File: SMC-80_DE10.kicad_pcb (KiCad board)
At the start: 4 copper layers, 51.8 x 47.2 mm, 32 parts, among them J1 IDE, J2 Port A, J3 Arduino1, J4 DE10-Lite GPIO, J5 Arduino2, U1 SST39SF040, U2 Z84C0010AEG, U3 AS6C4008A-55ZIN, U4 Z84C4310AEG

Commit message: rotated layout
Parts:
- removed the C1 at (205.7, 121.5)
- removed the D1 at (204.5, 114.7)
- removed the J1 at (128.6, 84.1)
- removed the J2 at (161.2, 121.0)
- removed JP1: IDE PWR, Connector_PinHeader_2.54mm:PinHeader_1x02_P2.54mm_Vertical
- removed JP2: WR Ena, Connector_PinHeader_2.54mm:PinHeader_1x03_P2.54mm_Vertical
- removed the R1 at (221.5, 113.8)
- removed the R2 at (225.3, 121.4)
- removed the R3 at (216.3, 122.8)
- removed the R5 at (204.1, 112.3)
- removed RN1: 2K2, Resistor_SMD:R_Cat16-4
- added J4: Port A, Connector_PinHeader_2.54mm:PinHeader_1x06_P2.54mm_Vertical, F.Cu at (114.3, 91.4)
- added R10: 10K, Resistor_SMD:R_0603_1608Metric_Pad1.05x0.95mm_HandSolder, F.Cu at (166.4, 110.5)
- added R7: 10K, Resistor_SMD:R_0603_1608Metric_Pad1.05x0.95mm_HandSolder, F.Cu at (138.4, 119.4)
- added R9: 10K, Resistor_SMD:R_0603_1608Metric_Pad1.05x0.95mm_HandSolder, F.Cu at (149.9, 111.8)
- R4: value 10K -> 100K
- R8: value 100K -> 10K
- RN2: value 10K -> 2K2
- U4: moved to F.Cu
- moved R4 97.6 mm to (116.8, 94.0), turned to 180 degrees
- moved R6 87.6 mm to (127.0, 94.0), turned to 0 degrees
- moved C5 80.5 mm to (123.2, 96.5)
- moved D1 77.2 mm to (139.7, 91.4), turned to 180 degrees
- moved R3 69.4 mm to (129.5, 133.9), turned to 180 degrees
- moved R5 67.5 mm to (127.0, 96.5), turned to 180 degrees
- moved R1 66.8 mm to (143.5, 91.4)
- moved R8 60.2 mm to (138.4, 116.8)
- moved C4 55.1 mm to (129.5, 119.4)
- moved C3 53.7 mm to (134.6, 105.4), turned to 180 degrees
- moved U4 49.9 mm to (120.7, 105.4)
- moved J1 44.1 mm to (170.5, 140.1), turned to 0 degrees
- moved RN2 43.1 mm to (110.5, 99.1)
- moved R2 42.3 mm to (156.2, 134.6), turned to 180 degrees
- moved U1 41.5 mm to (143.5, 130.8)
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- renumbered C2 to C1, C3 to C2, C4 to C3, C5 to C4, C6 to C5, D2 to D1, J3 to J1, J4 to J2, J5 to J3, R7 to R1, R9 to R2, R10 to R3, R11 to R5
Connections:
- J1 pad 1: /~M1 -> Net-(J1-Pad1)
- J1 pad 10: /SIO_~CE -> /~MREQ
- J1 pad 2: /~MREQ -> Net-(J1-Pad2)
- J1 pad 5: /~IORQ -> Net-(J1-Pad5)
- J1 pad 6: /~HALT -> /A16
- J1 pad 7: /~WAIT -> /A17
- J1 pad 8: Net-(J3-Pad8) -> /A18
- J1 pad 9: Net-(J3-Pad9) -> /~HALT
- J2 pad 2: /~RESET -> /ROM_~CE
- J2 pad 25: /A16 -> /D0
- J2 pad 26: /A17 -> /~RESET
- J2 pad 27: /A18 -> /D2
- J2 pad 28: /ROM_~CE -> /D1
- J2 pad 31: /D0 -> /D4
- J2 pad 32: /D1 -> /D3
- J2 pad 33: /D2 -> /D6
- J2 pad 34: /D3 -> /D5
- J2 pad 35: /D4 -> Net-(J2-Pad35)
- J2 pad 36: /D5 -> /D7
- J2 pad 37: /D6 -> Net-(J2-Pad37)
- J2 pad 38: /D7 -> /CLK
- J2 pad 39: /CLK -> /CLK_U
- J2 pad 40: /IDE_~CE~ -> /SIO_~CE
- J3 pad 1: /CLK_U -> /~IORQ
- J3 pad 2: Net-(J5-Pad2) -> /~WAIT
- J3 pad 3: Net-(J5-Pad3) -> /~M1
- J3 pad 5: /~RTS -> Net-(J3-Pad5)
- J3 pad 6: /RX -> Net-(J3-Pad6)
- J3 pad 7: /TX -> Net-(J3-Pad7)
- J3 pad 8: /~CTS -> Net-(J3-Pad8)
- R4 pad 1: VCC -> Net-(J4-Pad2)
- R4 pad 2: Net-(J1-Pad38) -> VCC
- R6 pad 1: Net-(J2-Pad2) -> Net-(J4-Pad6)
- R6 pad 2: VCC -> GND
- R8 pad 1: Net-(J2-Pad6) -> /Ram Rom and CPU/~INT
- R8 pad 2: GND -> VCC
- RN2 pad 1: VCC -> Net-(J4-Pad2)
- RN2 pad 2: VCC -> Net-(J4-Pad4)
- RN2 pad 3: VCC -> Net-(J4-Pad5)
- RN2 pad 4: VCC -> Net-(J4-Pad6)
- RN2 pad 5: /Ram Rom and CPU/~NMI -> /Ram Rom and CPU/~CTS
- RN2 pad 6: /~WAIT -> /Ram Rom and CPU/TXA
- RN2 pad 7: /Ram Rom and CPU/~BUSRQ -> /Ram Rom and CPU/RX
- RN2 pad 8: /Ram Rom and CPU/~INT -> /Ram Rom and CPU/~RTS
- U1 pad 31: Net-(JP2-Pad2) -> /~WR
- U4 pad 2: /~RTS -> /Ram Rom and CPU/~RTS
- U4 pad 3: /~CTS -> /Ram Rom and CPU/~CTS
- U4 pad 41: /RX -> /Ram Rom and CPU/RX
- U4 pad 44: /TX -> /Ram Rom and CPU/TXA
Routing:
- net /A1: track 0.00 -> 129.3 mm, vias 0 -> 6
- net /A0: track 0.00 -> 128.5 mm, vias 0 -> 6
- net /A5: track 0.00 -> 126.9 mm, vias 0 -> 5
- net /A4: track 0.00 -> 124.3 mm, vias 0 -> 5
- net /A3: track 0.00 -> 116.3 mm, vias 0 -> 5
- net /A2: track 0.00 -> 114.1 mm, vias 0 -> 5
- net /D5: track 0.00 -> 113.1 mm, vias 0 -> 8
- net /D3: track 0.00 -> 107.8 mm, vias 0 -> 8
- net /D4: track 0.00 -> 102.2 mm, vias 0 -> 5
- net /A10: track 0.00 -> 93.6 mm, vias 0 -> 5
- net /A11: track 0.00 -> 92.2 mm, vias 0 -> 4
- net /A13: track 0.00 -> 85.8 mm, vias 0 -> 4
- net /D6: track 0.00 -> 84.0 mm, vias 0 -> 4
- net /A9: track 0.00 -> 83.4 mm, vias 0 -> 5
- net /A6: track 0.00 -> 83.3 mm, vias 0 -> 2
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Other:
- board size 51.8 x 47.2 mm -> 66 x 55.9 mm
- board text added: "CKU"
- board text added: "M1"
- board text added: "~HALT"
- board text added: "~IORQ"
- board text added: "~MREQ"
- board text added: "~WAIT"
- board text removed: "IDE Active"
- board text removed: "IDE Power"
- board text removed: "MISO"
- board text removed: "MOSI"
- board text removed: "ON"
- board text removed: "PWR"
- board text removed: "RX"
- board text removed: "SCK"
- board text removed: "SCL"
- board text removed: "SDA"
- board text removed: "SS"
- board text removed: "TX"
- board text removed: "~CTS"
- board text removed: "~IDE"
- board text removed: "~RTS"

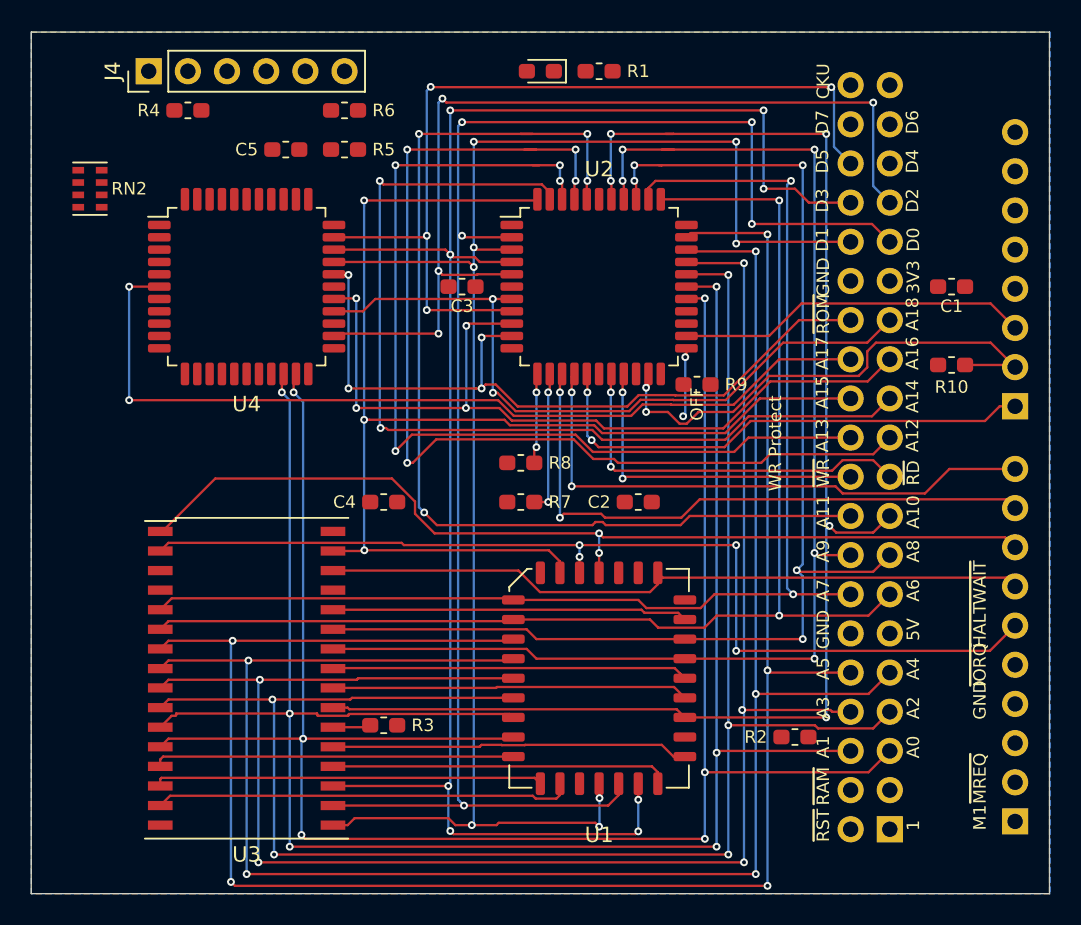
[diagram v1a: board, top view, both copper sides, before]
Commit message: Routing completed, fixed RAM/ROM paging
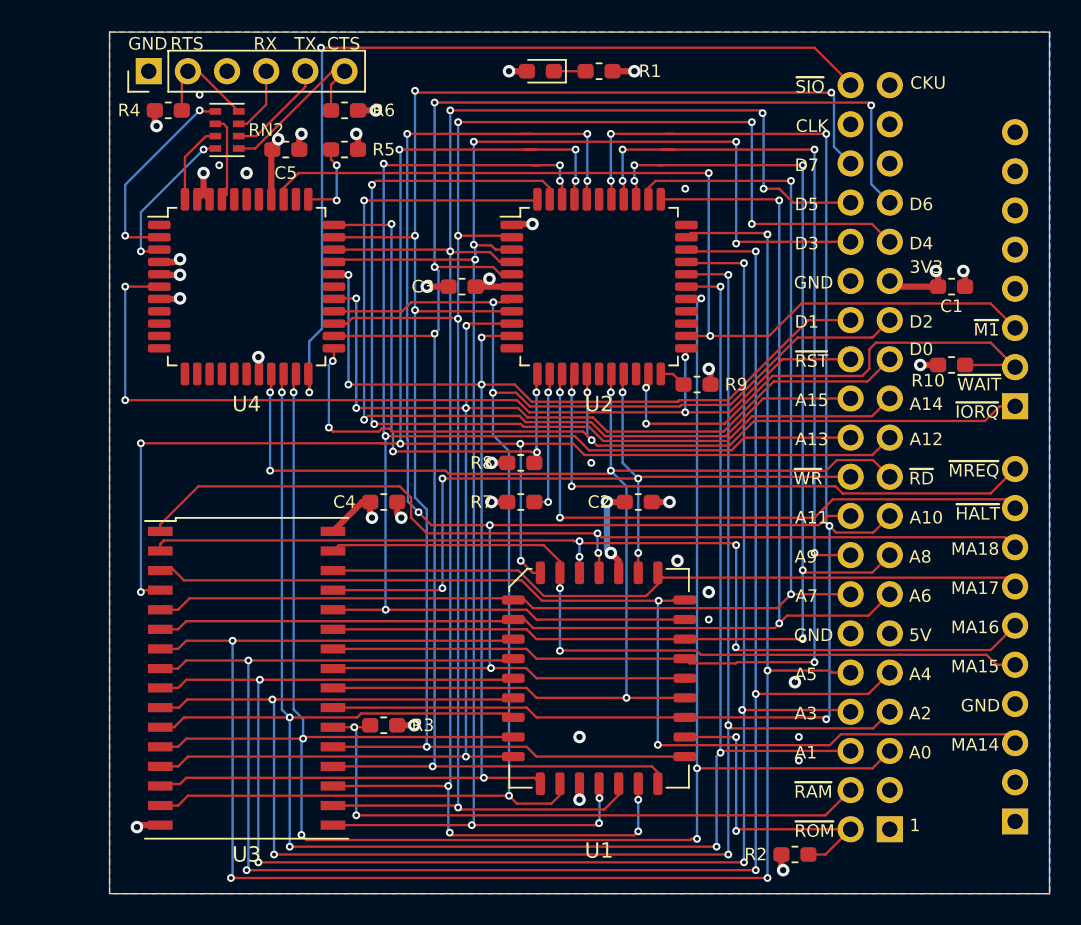
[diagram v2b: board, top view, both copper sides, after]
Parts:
- added G***: LOGO, Logos:asian_tiger, F.Cu at (134.4, 118.4)
- moved RN2 9.67 mm to (119.4, 95.2)
- moved R2 7.62 mm to (156.2, 142.2), turned to 0 degrees
- moved R4 1.27 mm to (115.6, 94.0)
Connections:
- net /A16 renamed /MA16
- net /A17 renamed /MA17
- net /A18 renamed /MA18
- J1 pad 1: Net-(J1-Pad1) -> (no net)
- J1 pad 2: Net-(J1-Pad2) -> (no net)
- J1 pad 3: Net-(J1-Pad3) -> /MA14
- J1 pad 5: Net-(J1-Pad5) -> /MA15
- J2 pad 1: Net-(J2-Pad1) -> (no net)
- J2 pad 11: +5V -> (no net)
- J2 pad 3: Net-(J2-Pad3) -> (no net)
- J2 pad 35: Net-(J2-Pad35) -> (no net)
- J2 pad 37: Net-(J2-Pad37) -> (no net)
- J3 pad 4: Net-(J3-Pad4) -> (no net)
- J3 pad 5: Net-(J3-Pad5) -> (no net)
- J3 pad 6: Net-(J3-Pad6) -> (no net)
- J3 pad 7: Net-(J3-Pad7) -> (no net)
- J3 pad 8: Net-(J3-Pad8) -> (no net)
- J4 pad 3: Net-(J4-Pad3) -> (no net)
- RN2 pad 1: Net-(J4-Pad2) -> /Ram Rom and CPU/~RTS
- RN2 pad 2: Net-(J4-Pad4) -> /Ram Rom and CPU/RX
- RN2 pad 3: Net-(J4-Pad5) -> /Ram Rom and CPU/TX
- RN2 pad 4: Net-(J4-Pad6) -> /Ram Rom and CPU/~CTS
- RN2 pad 5: /Ram Rom and CPU/~CTS -> Net-(J4-Pad6)
- RN2 pad 6: /Ram Rom and CPU/TXA -> Net-(J4-Pad5)
- RN2 pad 7: /Ram Rom and CPU/RX -> Net-(J4-Pad4)
- RN2 pad 8: /Ram Rom and CPU/~RTS -> Net-(J4-Pad2)
- U1 pad 29: /A14 -> /MA14
- U1 pad 3: /A15 -> /MA15
- U2 pad 11: Net-(U2-Pad11) -> (no net)
- U2 pad 17: Net-(U2-Pad17) -> (no net)
- U2 pad 20: Net-(U2-Pad20) -> (no net)
- U2 pad 25: Net-(U2-Pad25) -> (no net)
- U2 pad 33: Net-(U2-Pad33) -> (no net)
- U2 pad 39: Net-(U2-Pad39) -> (no net)
- U3 pad 3: /A14 -> /MA14
- U3 pad 31: /A15 -> /MA15
- U4 pad 1: Net-(U4-Pad1) -> (no net)
- U4 pad 10: Net-(U4-Pad10) -> (no net)
- U4 pad 11: Net-(U4-Pad11) -> (no net)
- U4 pad 12: Net-(U4-Pad12) -> (no net)
- U4 pad 13: Net-(U4-Pad13) -> (no net)
- U4 pad 14: Net-(U4-Pad14) -> (no net)
- U4 pad 15: Net-(U4-Pad15) -> (no net)
- U4 pad 16: Net-(U4-Pad16) -> (no net)
- U4 pad 17: Net-(U4-Pad17) -> (no net)
- U4 pad 28: Net-(U4-Pad28) -> (no net)
- U4 pad 35: Net-(U4-Pad35) -> (no net)
- U4 pad 38: Net-(U4-Pad38) -> (no net)
- U4 pad 39: Net-(U4-Pad39) -> (no net)
- U4 pad 40: Net-(U4-Pad40) -> (no net)
- U4 pad 44: /Ram Rom and CPU/TXA -> /Ram Rom and CPU/TX
- U4 pad 8: Net-(U4-Pad8) -> (no net)
- U4 pad 9: Net-(U4-Pad9) -> (no net)
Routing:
- net /MA14: track 0.00 -> 68.0 mm, vias 0 -> 2
- net /SIO_~CE: track 0.00 -> 59.3 mm, vias 0 -> 2
- net /MA15: track 0.00 -> 51.0 mm, vias 0 -> 2
- net /CLK: track 0.00 -> 50.9 mm, vias 0 -> 2
- net /CLK_U: track 0.00 -> 49.9 mm, vias 0 -> 1
- net /~RD: track 48.1 -> 91.9 mm, vias 2 -> 5
- net /~M1: track 22.8 -> 62.2 mm, vias 0 -> 2
- net /RAM_~CE: track 2.47 -> 41.0 mm, vias 0 -> 2
- net /A12: track 68.5 -> 104.0 mm, vias 4 -> 8
- net /~WR: track 21.7 -> 54.1 mm, vias 2 -> 5
- net VCC: track 0.00 -> 32.0 mm, vias 0 -> 15
- net /D7: track 80.9 -> 109.7 mm, vias 4 -> 5
- net /D6: track 84.0 -> 112.3 mm, vias 4 -> 5
- net /Ram Rom and CPU/~INT: track 5.85 -> 33.8 mm, vias 2 -> 4
- net /D2: track 73.7 -> 100.1 mm, vias 2 -> 3
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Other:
- board size 66 x 55.9 mm -> 61 x 55.9 mm
- board text added: "CLK"
- board text added: "CTS"
- board text added: "MA14"
- board text added: "MA15"
- board text added: "MA16"
- board text added: "MA17"
- board text added: "MA18"
- board text added: "RTS"
- board text added: "RX"
- board text added: "SMC-80 DE10-Lite Edition v1.0 by Hyiger Designs"
- board text added: "TX"
- board text added: "~M1"
- board text added: "~SIO"
- board text removed: "A16"
- board text removed: "A17"
- board text removed: "A18"
- board text removed: "DE10-Lite RAM/ROM/CF v1.0 by Hyiger Designs"
- board text removed: "M1"
- board text removed: "OFF"
- board text removed: "WR Protect"

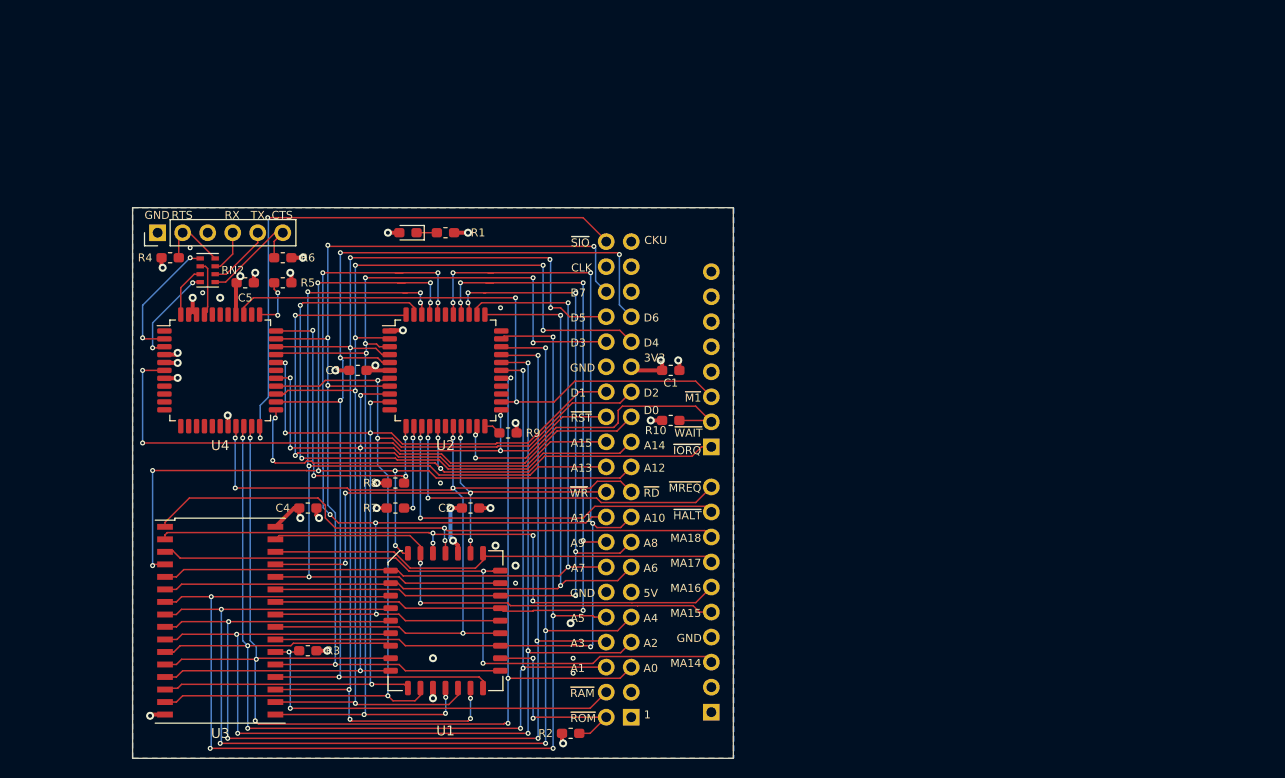
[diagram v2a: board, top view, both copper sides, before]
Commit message: added gnd plane stitching
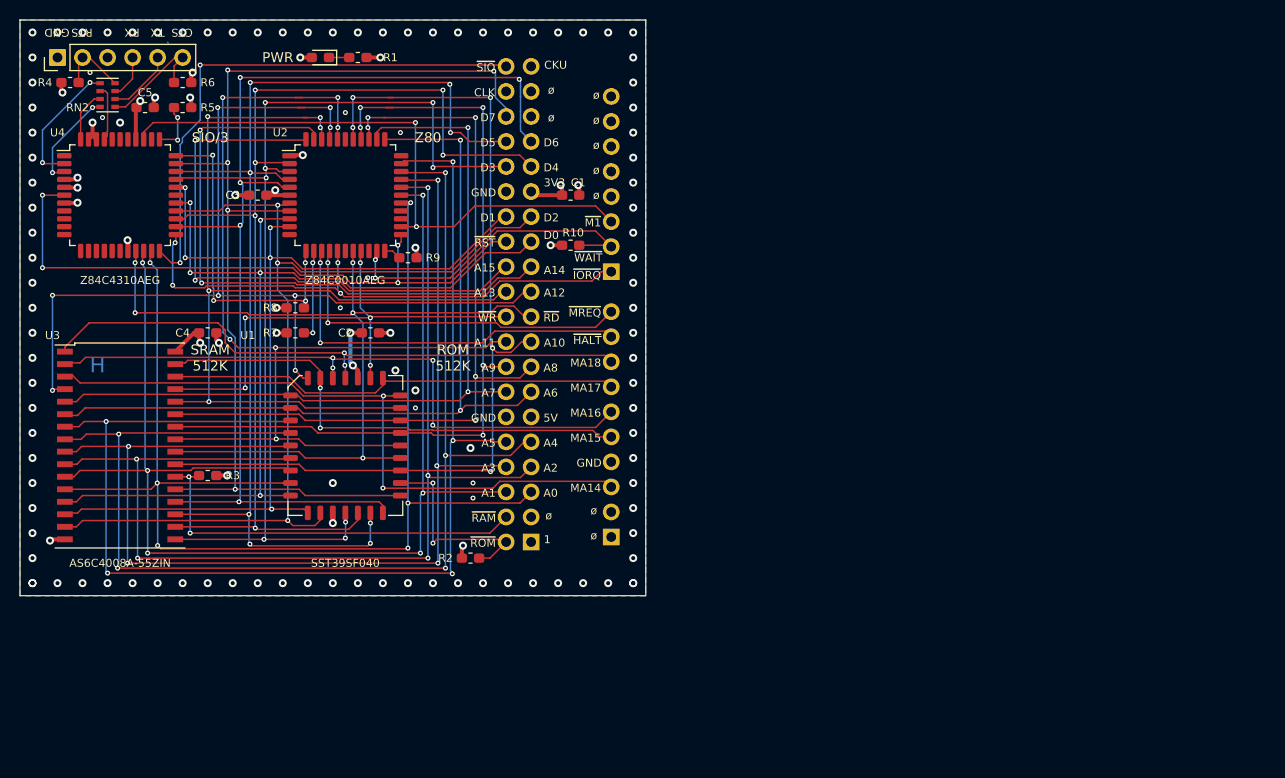
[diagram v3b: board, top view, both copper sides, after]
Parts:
- U1: footprint Package_LCC:PLCC-32_11.4x14.0mm_P1.27mm -> Package_LCC:PLCC-32_11.4x14.0mm_P1.27mm-Socket
- moved J2 20.5 mm to (152.2, 122.8)
- moved C2 20.5 mm to (135.9, 101.6)
- moved R9 20.5 mm to (139.7, 94.0)
- moved R2 20.5 mm to (146.1, 124.5)
- moved C3 20.5 mm to (124.5, 87.6)
- moved U3 20.5 mm to (110.5, 113.0)
- moved U4 20.5 mm to (110.5, 87.6)
- moved C1 20.5 mm to (156.2, 87.6)
- moved C4 20.5 mm to (119.4, 101.6)
- moved C5 20.5 mm to (113.0, 78.7)
- moved J1 20.5 mm to (160.3, 122.3)
- moved J3 20.5 mm to (160.3, 95.4)
- moved J4 20.5 mm to (104.1, 73.7)
- moved R10 20.5 mm to (156.2, 92.7)
- moved R3 20.5 mm to (119.4, 116.1)
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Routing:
- net /SIO_~CE: track 59.3 -> 54.8 mm
- net /~RESET: track 62.6 -> 64.0 mm
- net /~WAIT: track 34.1 -> 32.7 mm
- net /A5: track 126.0 -> 126.5 mm
- net GND: vias 24 -> 120
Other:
- board size 61 x 55.9 mm -> 63.5 x 58.4 mm
- board text added: "AS6C4008A-55ZIN"
- board text added: "H"
- board text added: "PWR"
- board text added: "ROM 512K"
- board text added: "SIO/3"
- board text added: "SRAM 512K"
- board text added: "SST39SF040"
- board text added: "Z80"
- board text added: "Z84C0010AEG"
- board text added: "Z84C4310AEG"
- board text added: "https://github.com/Hyiger-Designs/SMC-80_DE10"
- board text added: "ø"
